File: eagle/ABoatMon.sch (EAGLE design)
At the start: 25 parts, among them J1 5V, J2 GND, J3 GND

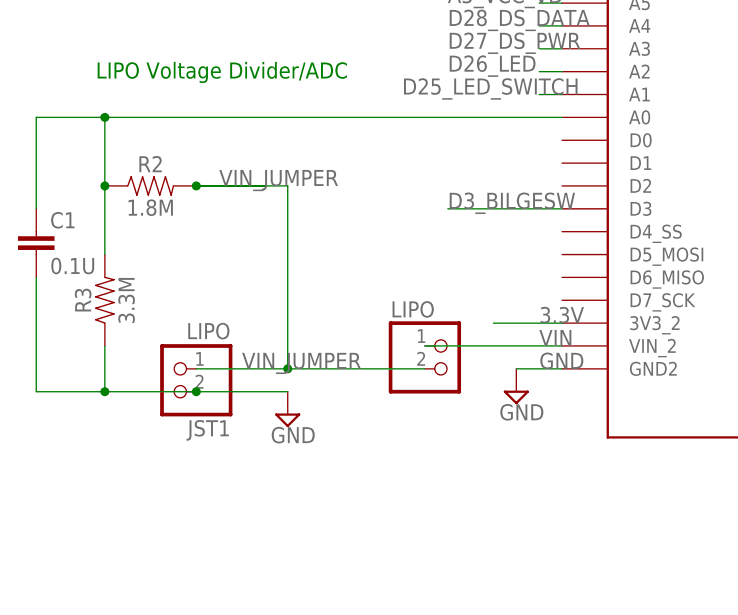
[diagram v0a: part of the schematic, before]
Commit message: LIPO jumper correction.  Reroute+better ground pours
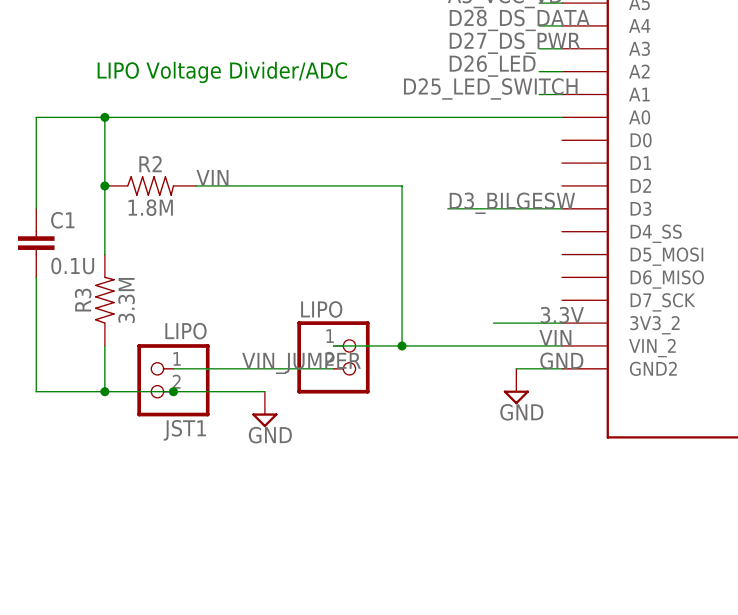
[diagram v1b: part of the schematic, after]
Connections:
- net VIN: now also R2.2
- net VIN_JUMPER: no longer R2.2
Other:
- moved on the sheet: JST1, LIPO
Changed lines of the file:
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@@
 <attributes>
 <attribute name="CNAME" value="MoteinoMega ABoatMon Shield"/>
-<attribute name="CREVISION" value="0.399"/>
+<attribute name="CREVISION" value="0.499"/>
 <attribute name="DESIGNER" value="gregcope@gmail.com"/>
 </attributes>
@@
 <attribute name="VALUE" x="146.05" y="114.3" size="1.778" layer="96"/>
 </instance>
-<instance part="JST1" gate="G$1" x="20.32" y="114.3" smashed="yes" rot="R180">
-<attribute name="NAME" x="26.67" y="108.585" size="1.778" layer="95" rot="R180"/>
-<attribute name="VALUE" x="26.67" y="119.38" size="1.778" layer="96" rot="R180"/>
-</instance>
-<instance part="SUPPLY2" gate="GND" x="33.02" y="109.22" smashed="yes">
-<attribute name="VALUE" x="31.115" y="106.045" size="1.778" layer="96"/>
+<instance part="JST1" gate="G$1" x="17.78" y="114.3" smashed="yes" rot="R180">
+<attribute name="NAME" x="24.13" y="108.585" size="1.778" layer="95" rot="R180"/>
+<attribute name="VALUE" x="24.13" y="119.38" size="1.778" layer="96" rot="R180"/>
+</instance>
+<instance part="SUPPLY2" gate="GND" x="30.48" y="109.22" smashed="yes">
+<attribute name="VALUE" x="28.575" y="106.045" size="1.778" layer="96"/>
 </instance>
 <instance part="FRAME1" gate="G$1" x="0" y="0" smashed="yes">
@@
 <attribute name="VALUE" x="166.37" y="73.66" size="1.778" layer="96"/>
 </instance>
-<instance part="LIPO" gate="G$1" x="50.8" y="114.3" smashed="yes">
-<attribute name="NAME" x="44.45" y="120.015" size="1.778" layer="95"/>
-<attribute name="VALUE" x="44.45" y="109.22" size="1.778" layer="96"/>
+<instance part="LIPO" gate="G$1" x="40.64" y="114.3" smashed="yes">
+<attribute name="NAME" x="34.29" y="120.015" size="1.778" layer="95"/>
+<attribute name="VALUE" x="34.29" y="109.22" size="1.778" layer="96"/>
 </instance>
 </instances>
@@
 <pinref part="JST1" gate="G$1" pin="1"/>
 <pinref part="SUPPLY2" gate="GND" pin="GND"/>
-<wire x1="22.86" y1="111.76" x2="33.02" y2="111.76" width="0.1524" layer="91"/>
+<wire x1="20.32" y1="111.76" x2="30.48" y2="111.76" width="0.1524" layer="91"/>
 <wire x1="12.7" y1="116.84" x2="12.7" y2="111.76" width="0.1524" layer="91"/>
 <wire x1="12.7" y1="111.76" x2="5.08" y2="111.76" width="0.1524" layer="91"/>
 <wire x1="5.08" y1="111.76" x2="5.08" y2="124.46" width="0.1524" layer="91"/>
-<wire x1="12.7" y1="111.76" x2="22.86" y2="111.76" width="0.1524" layer="91"/>
+<wire x1="12.7" y1="111.76" x2="20.32" y2="111.76" width="0.1524" layer="91"/>
 <junction x="12.7" y="111.76"/>
-<junction x="22.86" y="111.76"/>
+<junction x="20.32" y="111.76"/>
 <pinref part="C1" gate="G$1" pin="2"/>
 <pinref part="R3" gate="G$1" pin="1"/>
@@
 <pinref part="MOTEINO_MEGA" gate="G$1" pin="VIN_2"/>
 <pinref part="LIPO" gate="G$1" pin="1"/>
-<wire x1="63.5" y1="116.84" x2="48.26" y2="116.84" width="0.1524" layer="91"/>
+<wire x1="63.5" y1="116.84" x2="45.72" y2="116.84" width="0.1524" layer="91"/>
+<pinref part="R2" gate="G$1" pin="2"/>
+<wire x1="45.72" y1="116.84" x2="38.1" y2="116.84" width="0.1524" layer="91"/>
+<wire x1="22.86" y1="134.62" x2="45.72" y2="134.62" width="0.1524" layer="91"/>
+<wire x1="45.72" y1="134.62" x2="45.72" y2="116.84" width="0.1524" layer="91"/>
+<junction x="45.72" y="116.84"/>
+<label x="22.86" y="134.62" size="1.778" layer="95"/>
 </segment>
 </net>
@@
 <net name="VIN_JUMPER" class="1">
 <segment>
-<wire x1="30.48" y1="134.62" x2="22.86" y2="134.62" width="0.1524" layer="91"/>
-<wire x1="22.86" y1="134.62" x2="33.02" y2="134.62" width="0.1524" layer="91"/>
-<wire x1="33.02" y1="134.62" x2="33.02" y2="114.3" width="0.1524" layer="91"/>
 <label x="27.94" y="114.3" size="1.778" layer="95"/>
-<label x="25.4" y="134.62" size="1.778" layer="95"/>
-<pinref part="R2" gate="G$1" pin="2"/>
-<junction x="22.86" y="134.62"/>
 <pinref part="JST1" gate="G$1" pin="2"/>
 <pinref part="LIPO" gate="G$1" pin="2"/>
-<wire x1="22.86" y1="114.3" x2="33.02" y2="114.3" width="0.1524" layer="91"/>
-<wire x1="33.02" y1="114.3" x2="48.26" y2="114.3" width="0.1524" layer="91"/>
-<junction x="33.02" y="114.3"/>
-</segment>
-</net>
+<wire x1="20.32" y1="114.3" x2="38.1" y2="114.3" width="0.1524" layer="91"/>
+</segment>
+</net>

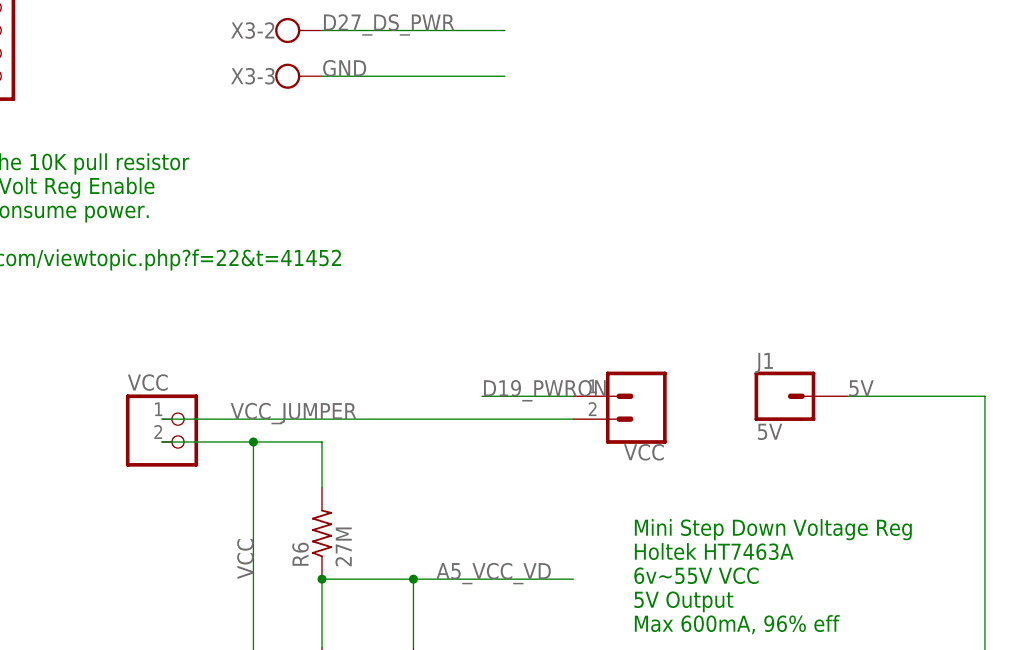
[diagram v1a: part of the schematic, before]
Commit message: Doh. fona swapped round, VCC header fix, better GND pour
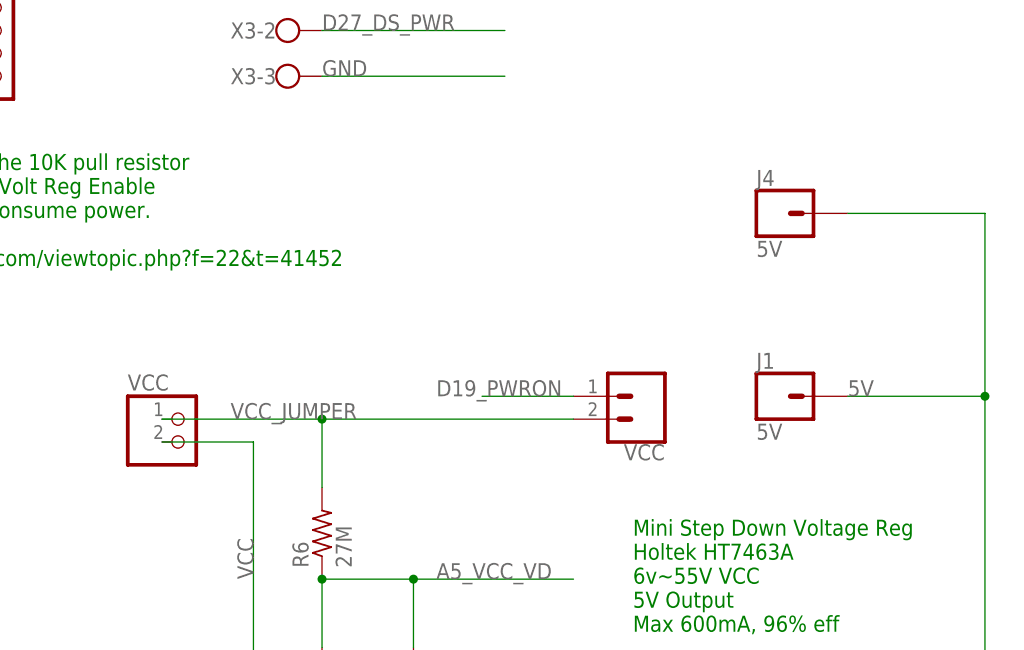
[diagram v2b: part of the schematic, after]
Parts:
- added J4: 5V, SparkFun-Connectors:CONN_01
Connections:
- net 5V: now also J4.1
- net VCC: no longer R6.2
- net VCC_JUMPER: now also R6.2
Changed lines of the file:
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@@
 <attributes>
 <attribute name="CNAME" value="MoteinoMega ABoatMon Shield"/>
-<attribute name="CREVISION" value="0.499"/>
+<attribute name="CREVISION" value="0.549"/>
 <attribute name="DESIGNER" value="gregcope@gmail.com"/>
 </attributes>
@@
 <part name="VCC" library="microbuilder" deviceset="HEADER-1X2" device="ROUND"/>
 <part name="LIPO" library="microbuilder" deviceset="HEADER-1X2" device="ROUND"/>
+<part name="J4" library="SparkFun-Connectors" deviceset="CONN_01" device="" value="5V"/>
 </parts>
 <sheets>
@@
 <attribute name="VALUE" x="34.29" y="109.22" size="1.778" layer="96"/>
 </instance>
+<instance part="J4" gate="G$1" x="238.76" y="104.14" smashed="yes">
+<attribute name="VALUE" x="236.22" y="99.314" size="1.778" layer="96" font="vector"/>
+<attribute name="NAME" x="236.22" y="107.188" size="1.778" layer="95" font="vector"/>
+</instance>
 </instances>
 <busses>
@@
 <pinref part="ENABLE" gate="G$1" pin="1"/>
 <wire x1="215.9" y1="83.82" x2="205.74" y2="83.82" width="0.1524" layer="91"/>
-<label x="205.74" y="83.82" size="1.778" layer="95"/>
+<label x="200.66" y="83.82" size="1.778" layer="95"/>
 </segment>
 </net>
@@
 <pinref part="VCC" gate="G$1" pin="2"/>
 <wire x1="170.18" y1="78.74" x2="180.34" y2="78.74" width="0.1524" layer="91"/>
-<pinref part="R6" gate="G$1" pin="2"/>
-<wire x1="180.34" y1="78.74" x2="187.96" y2="78.74" width="0.1524" layer="91"/>
-<wire x1="187.96" y1="78.74" x2="187.96" y2="73.66" width="0.1524" layer="91"/>
-<junction x="180.34" y="78.74"/>
 </segment>
 </net>
@@
 <pinref part="J1" gate="G$1" pin="1"/>
 <pinref part="X4" gate="-3" pin="KL"/>
+<pinref part="J4" gate="G$1" pin="1"/>
+<wire x1="246.38" y1="104.14" x2="261.62" y2="104.14" width="0.1524" layer="91"/>
+<wire x1="261.62" y1="104.14" x2="261.62" y2="83.82" width="0.1524" layer="91"/>
+<junction x="261.62" y="83.82"/>
 </segment>
 </net>
@@
 <pinref part="ENABLE" gate="G$1" pin="2"/>
 <pinref part="VCC" gate="G$1" pin="1"/>
-<wire x1="215.9" y1="81.28" x2="170.18" y2="81.28" width="0.1524" layer="91"/>
+<wire x1="215.9" y1="81.28" x2="187.96" y2="81.28" width="0.1524" layer="91"/>
 <label x="177.8" y="81.28" size="1.778" layer="95"/>
-</segment>
-</net>
+<pinref part="R6" gate="G$1" pin="2"/>
+<wire x1="187.96" y1="81.28" x2="170.18" y2="81.28" width="0.1524" layer="91"/>
+<wire x1="187.96" y1="73.66" x2="187.96" y2="81.28" width="0.1524" layer="91"/>
+<junction x="187.96" y="81.28"/>
+</segment>
+</net>
